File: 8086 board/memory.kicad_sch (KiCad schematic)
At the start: 49 parts, among them U10 74AC373, U11 74HC138, U12 74HC138, U13 CXK58257AM, U14 IS61C256AH, U15 IS61C256AH, U16 IS61C256AH, U17 IS61C256AH, U18 IS61C3216, U19 AM29F002, U2 74AC00, U20 AM29F002, U21 28F400B5, U3 74HC14, U8 74AC373, U9 74AC373

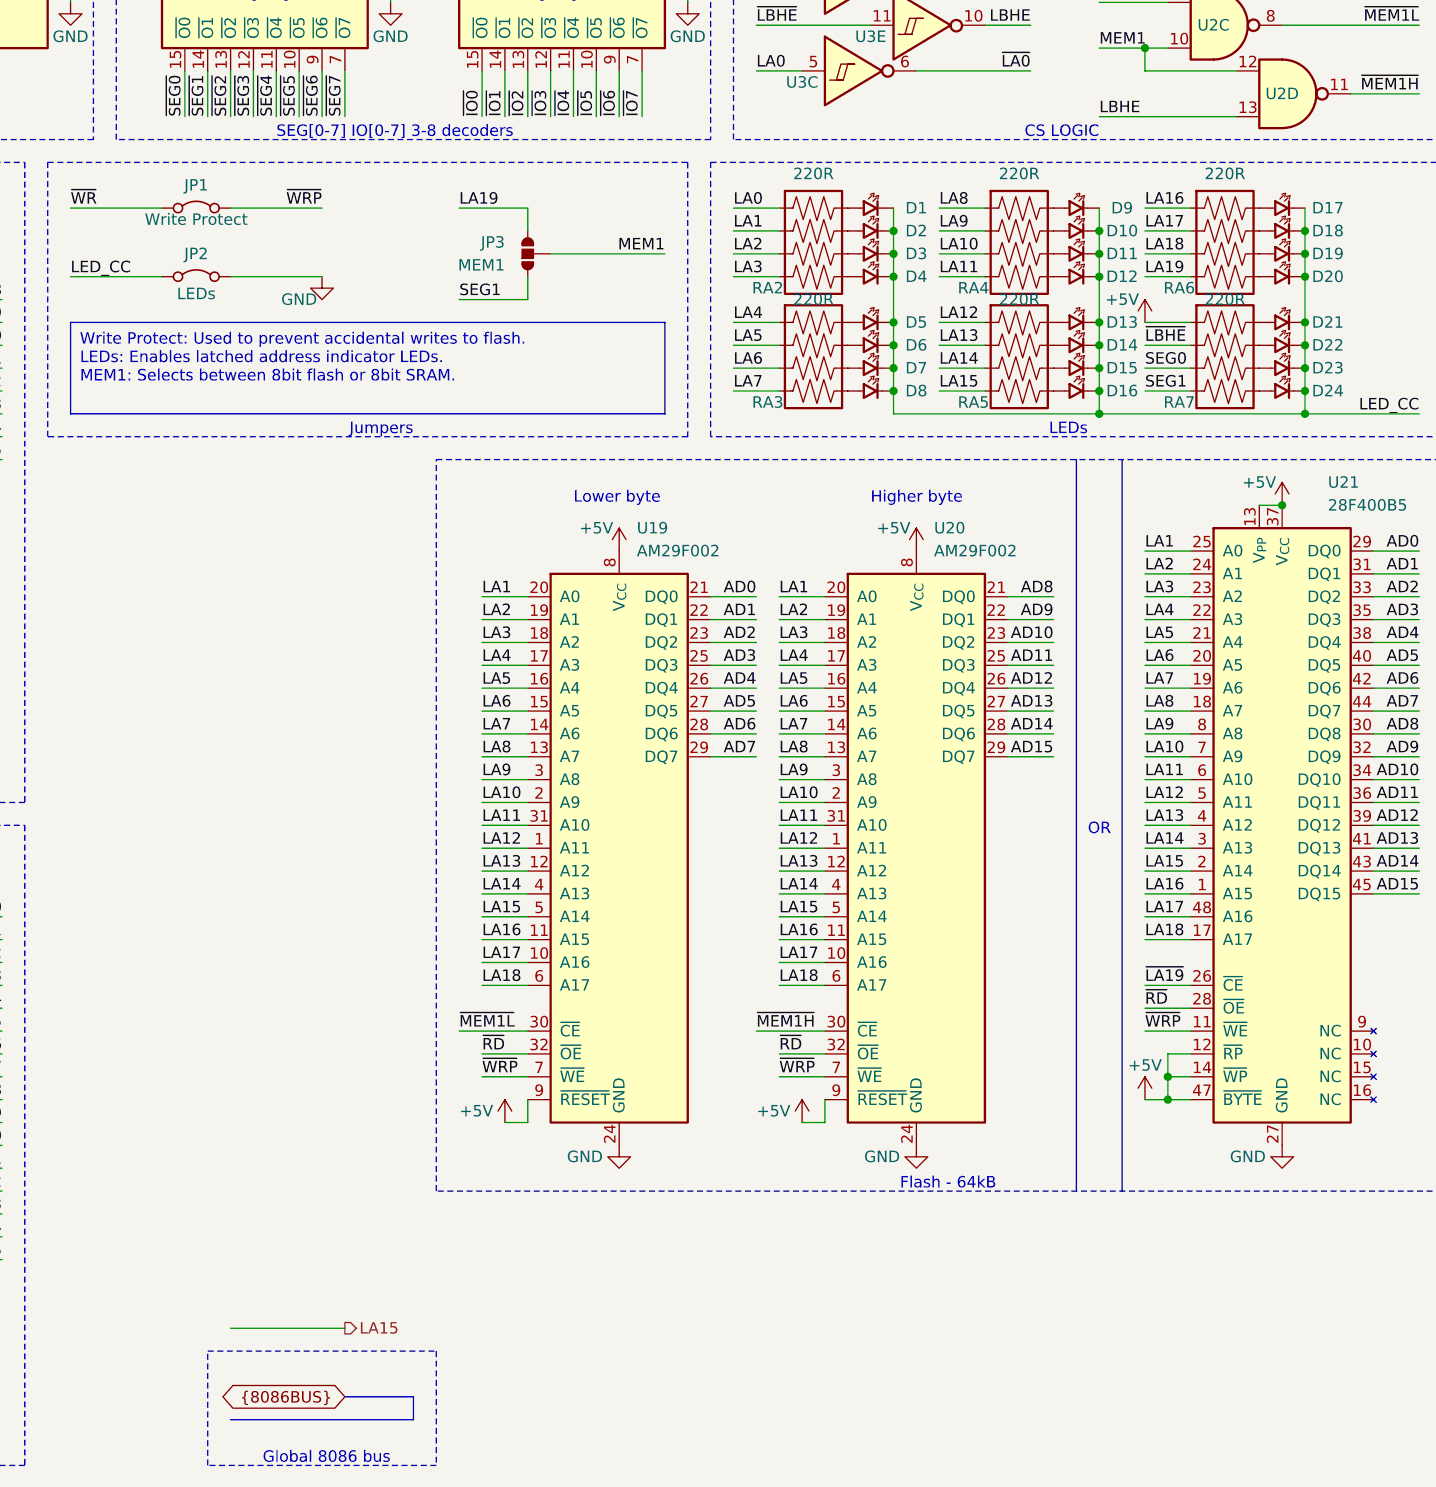
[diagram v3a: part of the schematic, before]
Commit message: change to 4 pin crystal
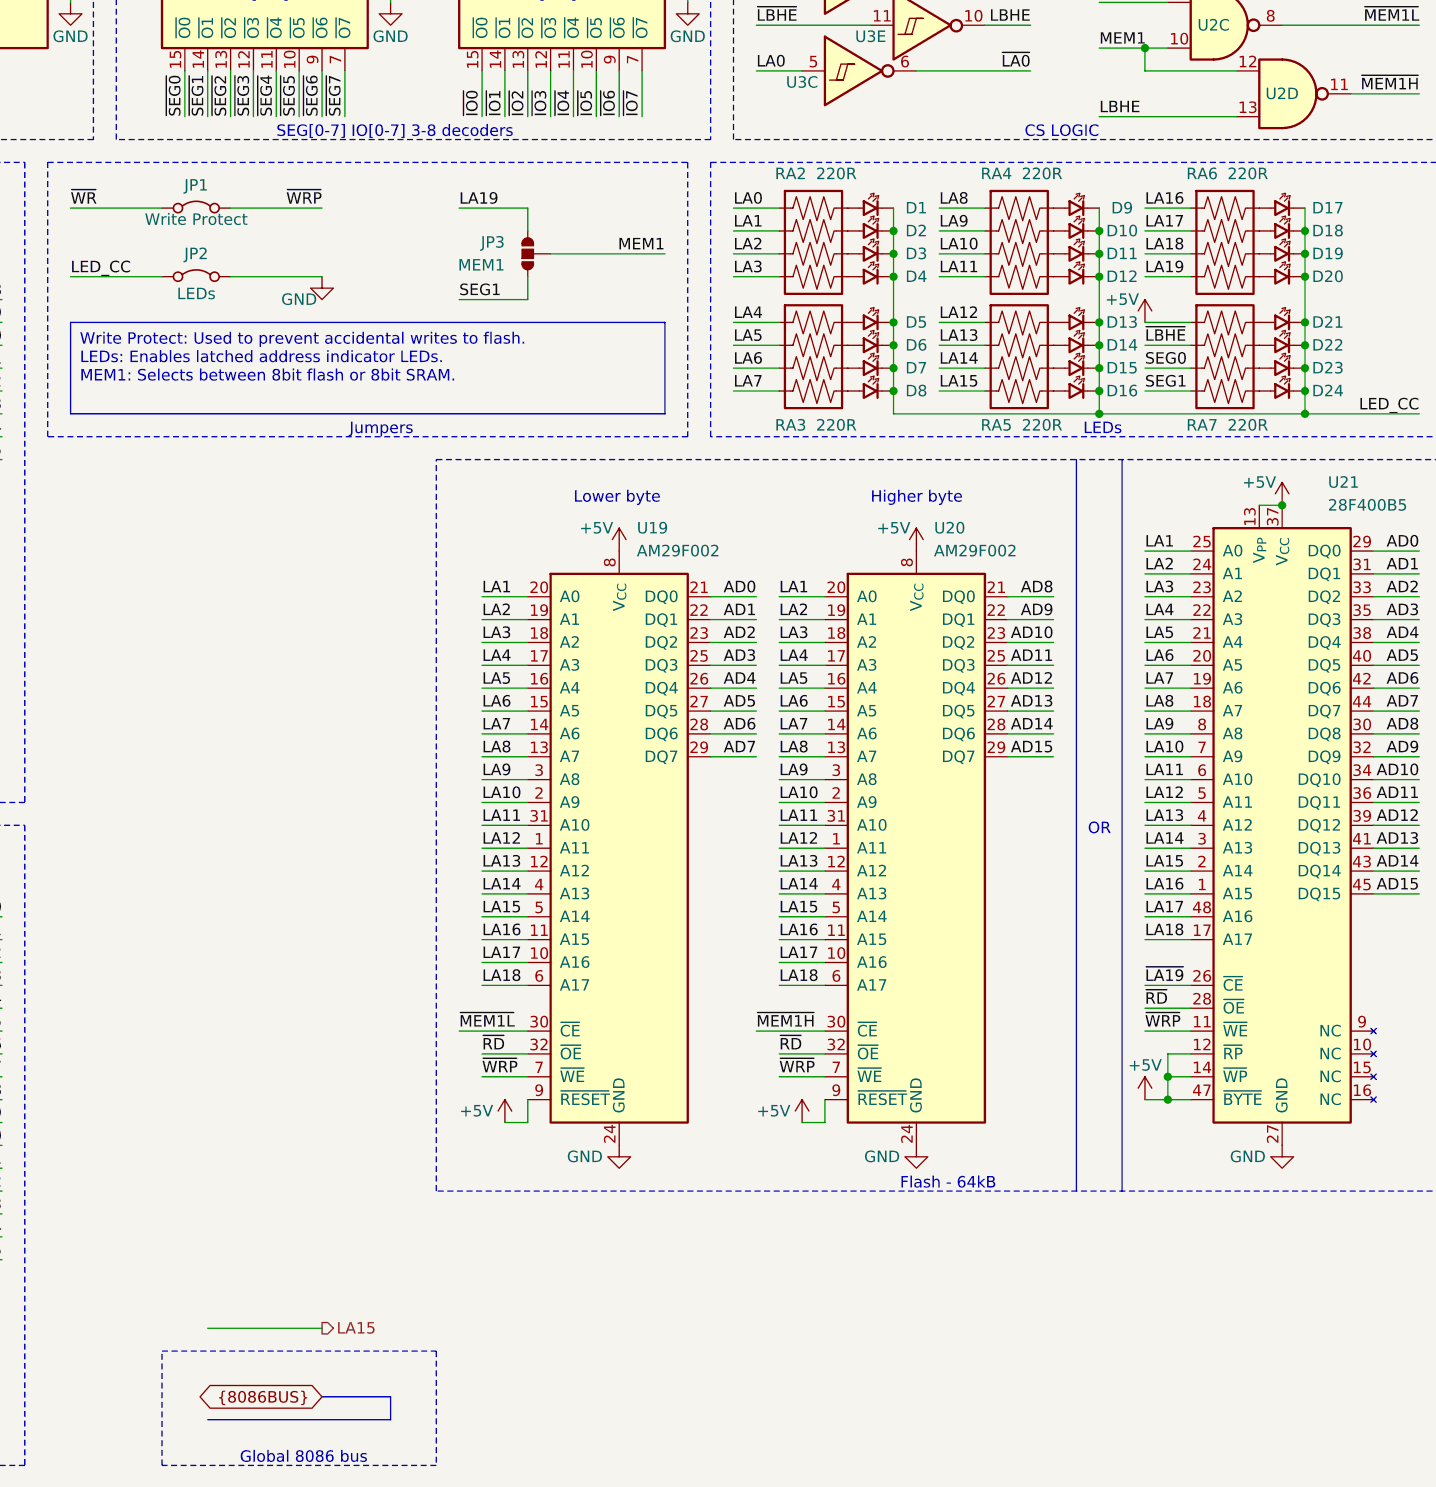
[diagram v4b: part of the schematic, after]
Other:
- company: (none) -> Eldad Hellerman
- title: (none) -> 8086 computer
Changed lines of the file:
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@@
 (kicad_sch (version 20230121) (generator eeschema)
   (paper "A4")
+  (title_block
+    (title "8086 computer")
+    (date "2023.10.26")
+    (rev "V1.0.0")
+    (company "Eldad Hellerman")
+    (comment 1 "Open Source: github.com/EldadHellerman/8086-computer")
+  )
   (junction (at 269.24 63.5) (diameter 0) (color 0 0 0 0)
   )
@@
     (stroke (width 0) (type default))
   )
-  (wire (pts (xy 149.86 180.34) (xy 162.56 180.34))
+  (wire (pts (xy 147.32 180.34) (xy 160.02 180.34))
     (stroke (width 0) (type default))
   )
@@
     (stroke (width 0) (type default))
   )
-  (bus (pts (xy 170.18 187.96) (xy 170.18 190.5))
+  (bus (pts (xy 167.64 187.96) (xy 167.64 190.5))
     (stroke (width 0) (type default))
   )
@@
     (stroke (width 0) (type default))
   )
-  (bus (pts (xy 149.86 190.5) (xy 170.18 190.5))
+  (bus (pts (xy 147.32 190.5) (xy 167.64 190.5))
     (stroke (width 0) (type default))
   )
@@
     (stroke (width 0) (type default))
   )
-  (bus (pts (xy 162.56 187.96) (xy 170.18 187.96))
+  (bus (pts (xy 160.02 187.96) (xy 167.64 187.96))
     (stroke (width 0) (type default))
   )
@@
     (fill (type none))
   )
-  (rectangle (start 147.32 182.88) (end 172.72 195.58)
+  (rectangle (start 142.24 182.88) (end 172.72 195.58)
     (stroke (width 0) (type dash))
     (fill (type none))
@@
     (effects (font (size 1.27 1.27)) (justify left bottom))
   )
-  (text "LEDs" (at 245.11 81.28 0)
+  (text "LEDs" (at 248.92 81.28 0)
     (effects (font (size 1.27 1.27)) (justify right bottom))
   )
@@
     (effects (font (size 1.27 1.27)) (justify right bottom))
   )
-  (text "Global 8086 bus" (at 167.64 195.58 0)
+  (text "Global 8086 bus" (at 165.1 195.58 0)
     (effects (font (size 1.27 1.27)) (justify right bottom))
   )
@@
     (effects (font (size 1.27 1.27)) (justify left bottom))
   )
-  (global_label "{8086BUS}" (shape bidirectional) (at 162.56 187.96 180) (fields_autoplaced)
+  (global_label "{8086BUS}" (shape bidirectional) (at 160.02 187.96 180) (fields_autoplaced)
     (effects (font (size 1.27 1.27)) (justify right))
-    (property "Intersheetrefs" "${INTERSHEET_REFS}" (at 148.2015 187.96 0)
+    (property "Intersheetrefs" "${INTERSHEET_REFS}" (at 145.6615 187.96 0)
       (effects (font (size 1.27 1.27)) (justify right) hide)
     )
   )
-  (hierarchical_label "LA15" (shape output) (at 162.56 180.34 0) (fields_autoplaced)
+  (hierarchical_label "LA15" (shape output) (at 160.02 180.34 0) (fields_autoplaced)
     (effects (font (size 1.27 1.27)) (justify left))
   )
@@
   (symbol (lib_id "8086PC:R_Array_4") (at 213.36 58.42 0) (unit 1)
     (in_bom yes) (on_board yes) (dnp no)
-    (property "Reference" "RA2" (at 209.55 64.77 0)
+    (property "Reference" "RA2" (at 212.09 52.07 0)
       (effects (font (size 1.27 1.27)))
     )
-    (property "Value" "220R" (at 214.63 52.07 0)
+    (property "Value" "220R" (at 217.17 52.07 0)
       (effects (font (size 1.27 1.27)))
     )
@@
   (symbol (lib_id "8086PC:R_Array_4") (at 213.36 71.12 0) (unit 1)
     (in_bom yes) (on_board yes) (dnp no)
-    (property "Reference" "RA3" (at 209.55 77.47 0)
+    (property "Reference" "RA3" (at 212.09 80.01 0)
       (effects (font (size 1.27 1.27)))
     )
-    (property "Value" "220R" (at 214.63 66.04 0)
+    (property "Value" "220R" (at 217.17 80.01 0)
       (effects (font (size 1.27 1.27)))
     )
@@
   (symbol (lib_id "8086PC:R_Array_4") (at 259.08 58.42 0) (unit 1)
     (in_bom yes) (on_board yes) (dnp no)
-    (property "Reference" "RA6" (at 255.27 64.77 0)
+    (property "Reference" "RA6" (at 257.81 52.07 0)
       (effects (font (size 1.27 1.27)))
     )
-    (property "Value" "220R" (at 260.35 52.07 0)
+    (property "Value" "220R" (at 262.89 52.07 0)
       (effects (font (size 1.27 1.27)))
     )
@@
   (symbol (lib_id "8086PC:R_Array_4") (at 236.22 71.12 0) (unit 1)
     (in_bom yes) (on_board yes) (dnp no)
-    (property "Reference" "RA5" (at 232.41 77.47 0)
+    (property "Reference" "RA5" (at 234.95 80.01 0)
       (effects (font (size 1.27 1.27)))
     )
-    (property "Value" "220R" (at 237.49 66.04 0)
+    (property "Value" "220R" (at 240.03 80.01 0)
       (effects (font (size 1.27 1.27)))
     )
@@
   (symbol (lib_id "8086PC:R_Array_4") (at 259.08 71.12 0) (unit 1)
     (in_bom yes) (on_board yes) (dnp no)
-    (property "Reference" "RA7" (at 255.27 77.47 0)
+    (property "Reference" "RA7" (at 257.81 80.01 0)
       (effects (font (size 1.27 1.27)))
     )
-    (property "Value" "220R" (at 260.35 66.04 0)
+    (property "Value" "220R" (at 262.89 80.01 0)
       (effects (font (size 1.27 1.27)))
     )
@@
   (symbol (lib_id "8086PC:R_Array_4") (at 236.22 58.42 0) (unit 1)
     (in_bom yes) (on_board yes) (dnp no)
-    (property "Reference" "RA4" (at 232.41 64.77 0)
+    (property "Reference" "RA4" (at 234.95 52.07 0)
       (effects (font (size 1.27 1.27)))
     )
-    (property "Value" "220R" (at 237.49 52.07 0)
+    (property "Value" "220R" (at 240.03 52.07 0)
       (effects (font (size 1.27 1.27)))
     )

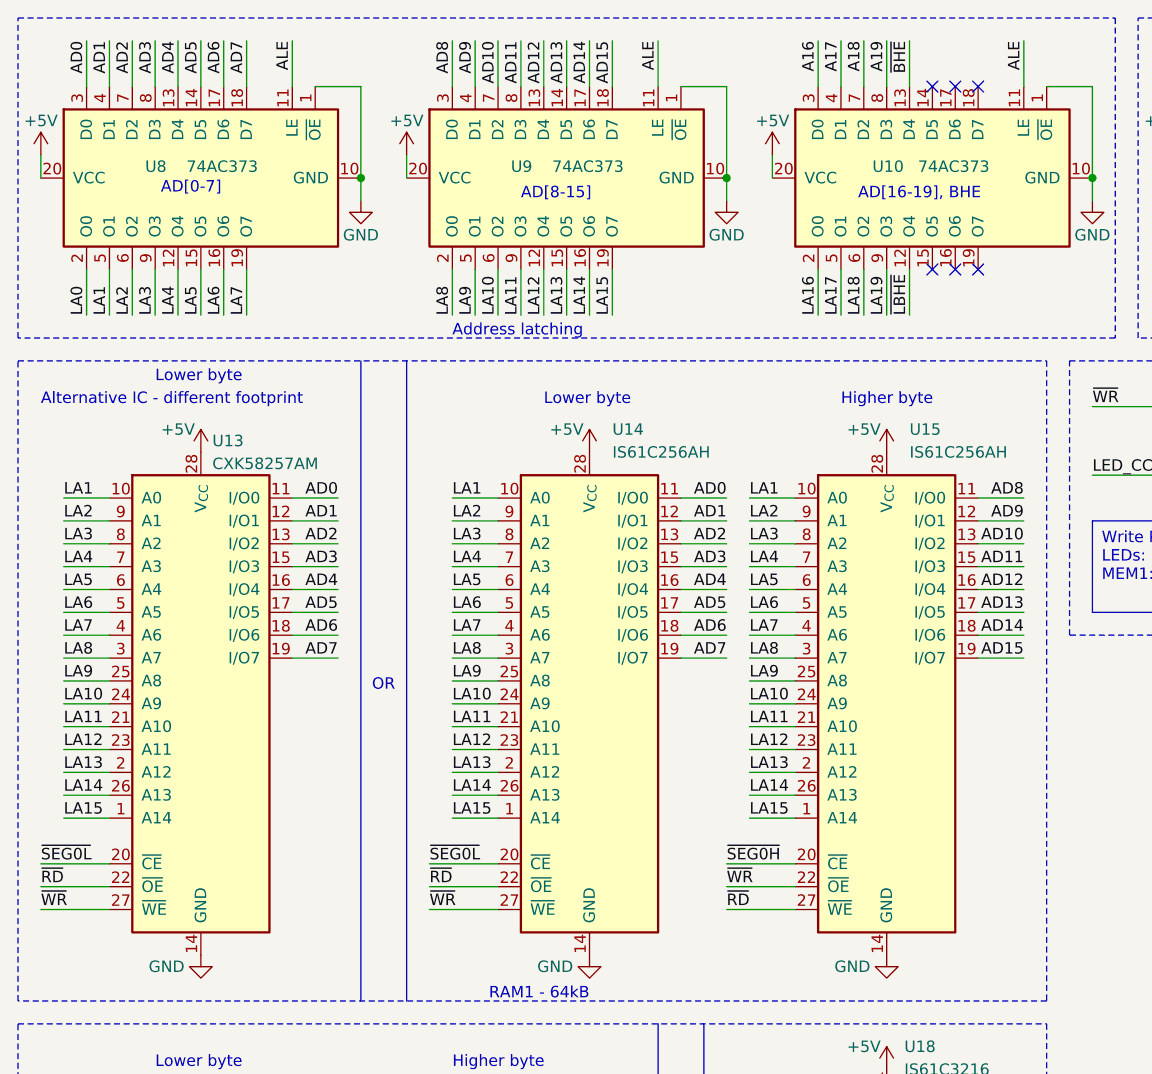
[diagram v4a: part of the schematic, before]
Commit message: change 74HC373D (SO20) to 74HC573PW (TSSOP20)
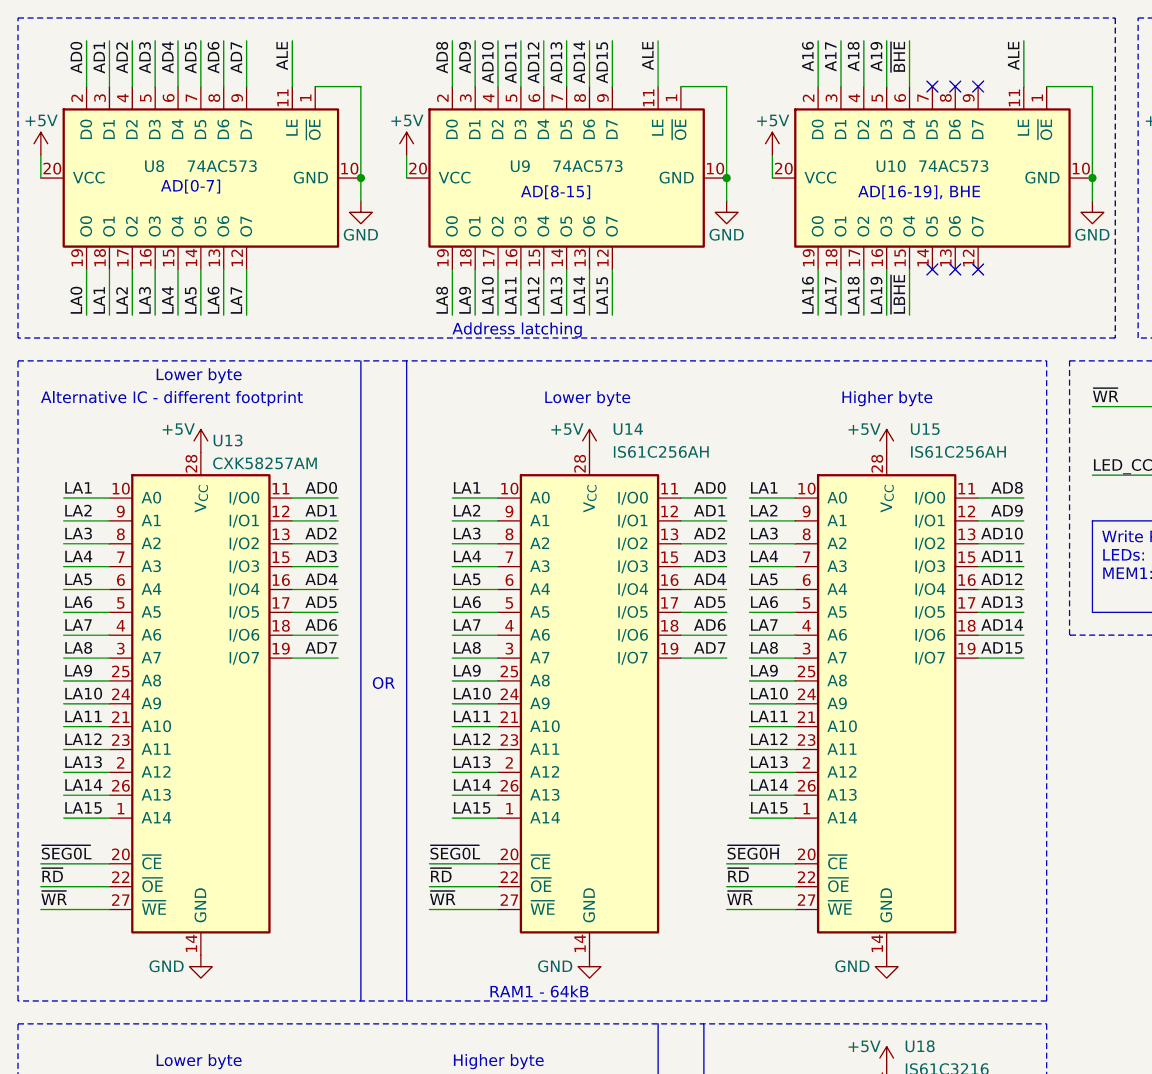
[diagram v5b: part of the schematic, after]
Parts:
- removed U10, U8, U9: 74AC373, Package_SO:SOIC-20W_7.5x12.8mm_P1.27mm, symbol 8086PC:74AC373
- added U10, U8, U9: 74AC573, Package_SO:TSSOP-20_4.4x6.5mm_P0.65mm, symbol 8086PC:74AC573
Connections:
- net +5V: now also U10.20 (VCC), U8.20 (VCC), U9.20 (VCC)
- net A16: now also U10.2 (D0)
- net A17: now also U10.3 (D1)
- net A18: now also U10.4 (D2)
- net A19: now also U10.5 (D3)
- net AD0: now also U8.2 (D0)
- net AD1: now also U8.3 (D1)
- net AD10: now also U9.4 (D2)
- net AD11: now also U9.5 (D3)
- net AD12: now also U9.6 (D4)
- net AD13: now also U9.7 (D5)
- net AD14: now also U9.8 (D6)
- net AD15: now also U9.9 (D7)
- net AD2: now also U8.4 (D2)
- net AD3: now also U8.5 (D3)
- net AD4: now also U8.6 (D4)
- net AD5: now also U8.7 (D5)
- net AD6: now also U8.8 (D6)
- net AD7: now also U8.9 (D7)
- net AD8: now also U9.2 (D0)
- net AD9: now also U9.3 (D1)
- net ALE: now also U10.11 (LE), U8.11 (LE), U9.11 (LE)
- net GND: now also U10.1 (~{OE}), U10.10 (GND), U8.1 (~{OE}), U8.10 (GND), U9.1 (~{OE}), U9.10 (GND)
- net LA0: now also U8.19 (O0)
- net LA1: now also U8.18 (O1)
- net LA10: now also U9.17 (O2)
- net LA11: now also U9.16 (O3)
- net LA12: now also U9.15 (O4)
- net LA13: now also U9.14 (O5)
- net LA14: now also U9.13 (O6)
- net LA15: now also U9.12 (O7)
- net LA16: now also U10.19 (O0)
- net LA17: now also U10.18 (O1)
- net LA18: now also U10.17 (O2)
- net LA19: now also U10.16 (O3)
- net LA2: now also U8.17 (O2)
- net LA3: now also U8.16 (O3)
- net LA4: now also U8.15 (O4)
- net LA5: now also U8.14 (O5)
- net LA6: now also U8.13 (O6)
- net LA7: now also U8.12 (O7)
- net LA8: now also U9.19 (O0)
- net LA9: now also U9.18 (O1)
- net ~{BHE}: now also U10.6 (D4)
- net ~{LBHE}: now also U10.15 (O4)
- net ~{RD}: now also U15.22 (~{OE}); no longer U15.27 (~{WE})
- net ~{WR}: now also U15.27 (~{WE}); no longer U15.22 (~{OE})
